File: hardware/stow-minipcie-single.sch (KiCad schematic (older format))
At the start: 2 parts

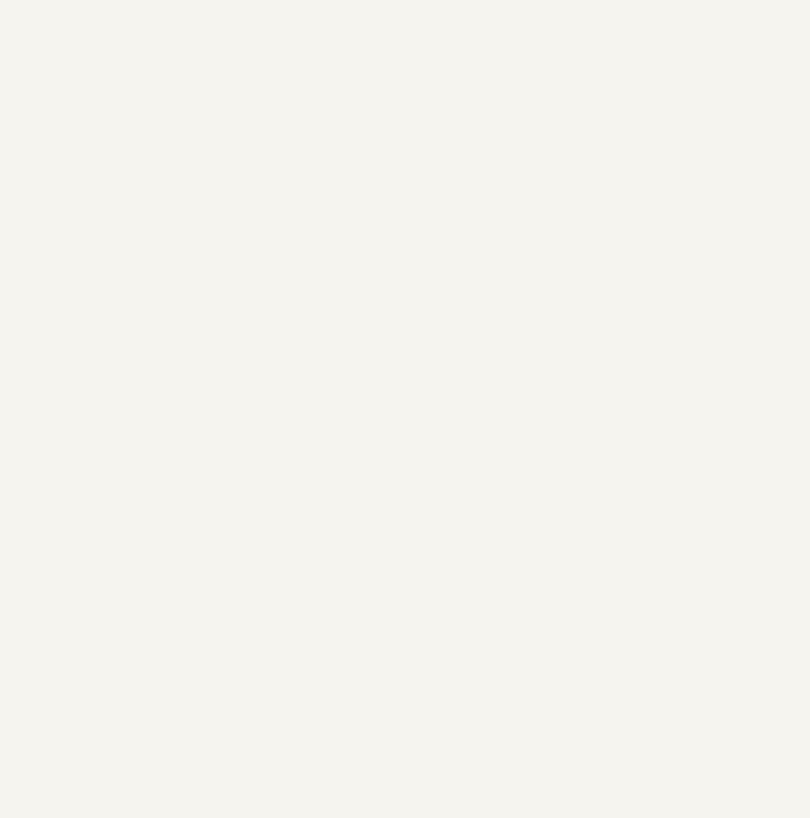
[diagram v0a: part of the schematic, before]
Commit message: Add FTDI chip to schematic.
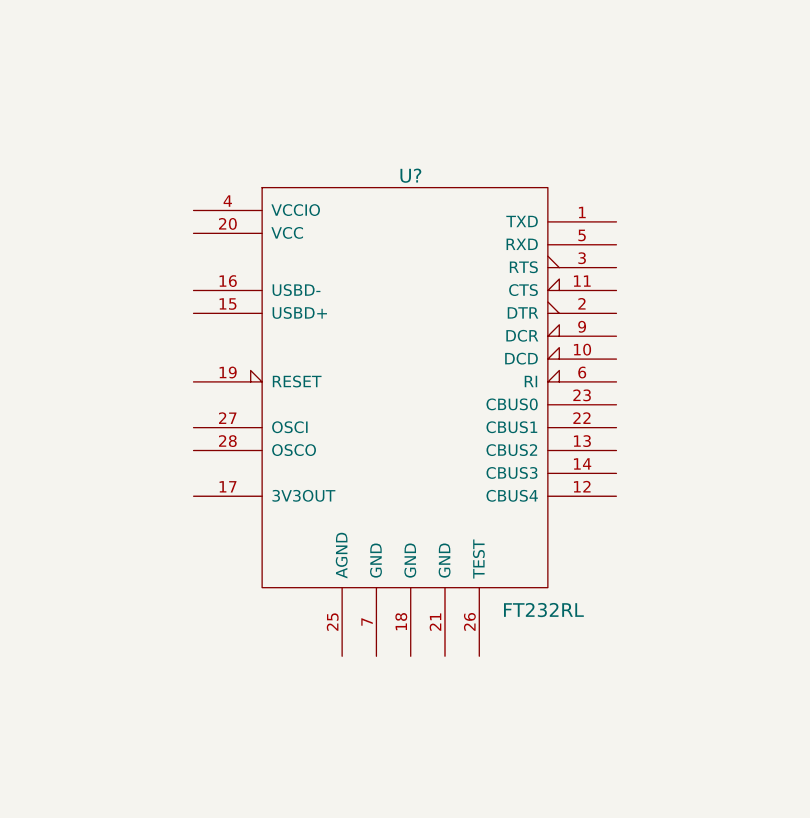
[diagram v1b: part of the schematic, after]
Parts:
- added U?: FT232RL, symbol FT232RL
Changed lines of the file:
@@
+	1    0    0    -1
+$EndComp
+$Comp
+L FT232RL U?
+U 1 1 55C1978C
+P 6150 3700
+F 0 "U?" H 6150 4600 60  0000 C CNN
+F 1 "FT232RL" H 6550 2700 60  0000 L CNN
+F 2 "" H 6150 3700 60  0000 C CNN
+F 3 "" H 6150 3700 60  0000 C CNN
+	1    6150 3700
 	1    0    0    -1
 $EndComp

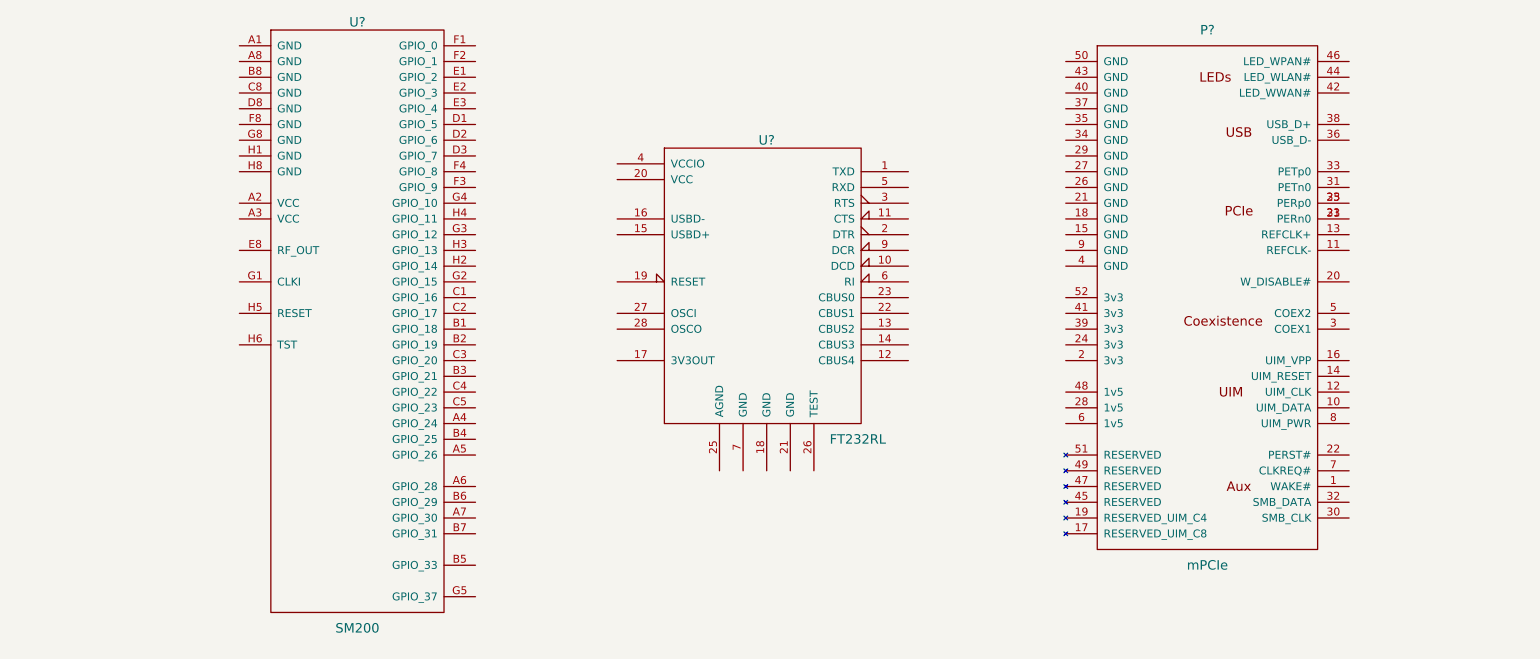
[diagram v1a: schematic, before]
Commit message: Add some schematic connections.
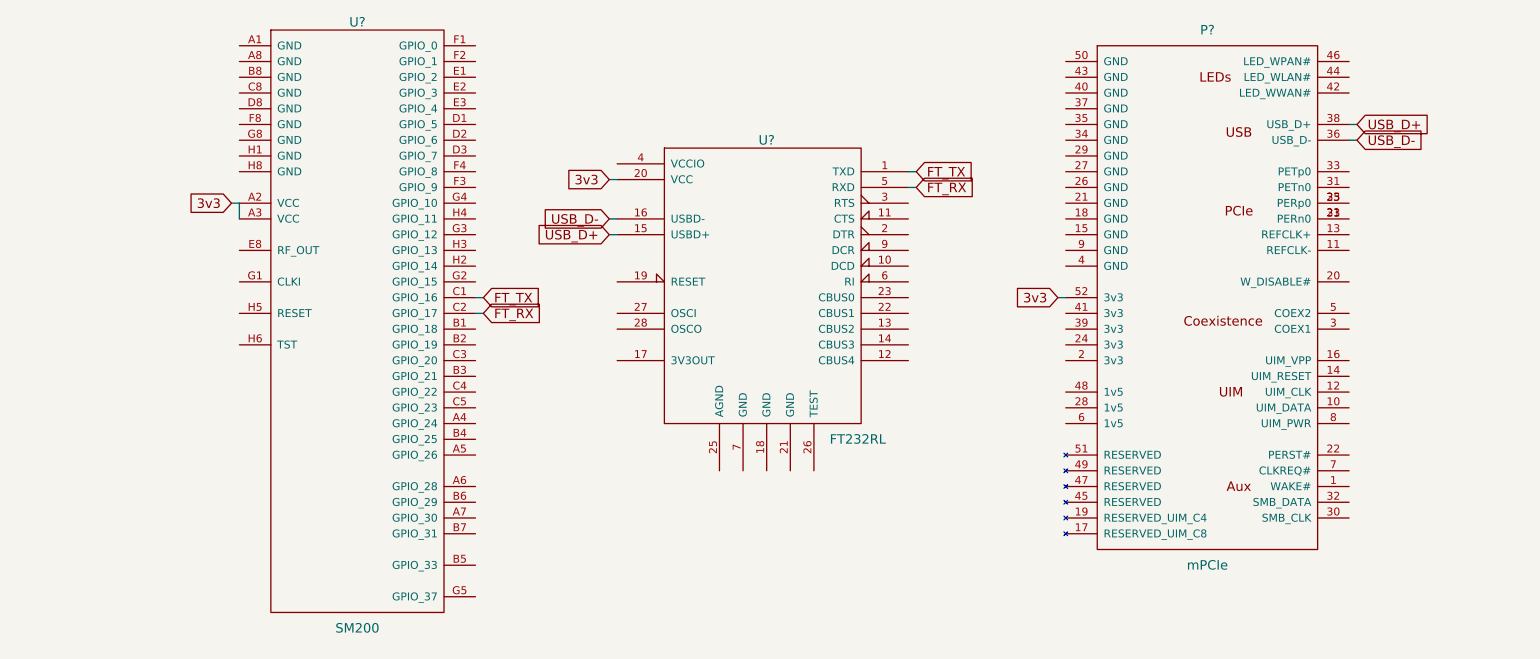
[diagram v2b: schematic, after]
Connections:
- net 3v3: now reaches U?.A2 (VCC)
- net 3v3: now also P?.52 (3v3), U?.20 (VCC), U?.A3 (VCC)
- net FT_TX: now reaches U?.C1 (GPIO_16)
- net FT_TX: now also U?.1 (TXD)
- net FT_RX: now reaches U?.C2 (GPIO_17)
- net FT_RX: now also U?.5 (RXD)
- net USB_D-: now reaches P?.36 (USB_D-)
- net USB_D-: now also U?.16 (USBD-)
- net USB_D+: now reaches P?.38 (USB_D+)
- net USB_D+: now also U?.15 (USBD+)
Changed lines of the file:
@@
 	1    0    0    -1
 $EndComp
+Text GLabel 9900 2700 2    60   Input ~ 0
+USB_D+
+Text GLabel 9900 2800 2    60   Input ~ 0
+USB_D-
+Text GLabel 5150 3400 0    60   Input ~ 0
+USB_D+
+Text GLabel 5150 3300 0    60   Input ~ 0
+USB_D-
+Text GLabel 5150 3050 0    60   Input ~ 0
+3v3
+Text GLabel 8000 3800 0    60   Input ~ 0
+3v3
+Text GLabel 2750 3200 0    60   Input ~ 0
+3v3
+Wire Wire Line
+	5150 3300 5200 3300
+Wire Wire Line
+	5150 3400 5200 3400
+Wire Wire Line
+	9850 2700 9900 2700
+Wire Wire Line
+	9850 2800 9900 2800
+Wire Wire Line
+	8000 3800 8050 3800
+Wire Wire Line
+	5150 3050 5200 3050
+Wire Wire Line
+	2750 3200 2800 3200
+Wire Wire Line
+	2800 3200 2800 3300
+Text GLabel 7100 3000 2    60   Input ~ 0
+FT_TX
+Text GLabel 7100 3100 2    60   Input ~ 0
+FT_RX
+Wire Wire Line
+	7050 3000 7100 3000
+Wire Wire Line
+	7100 3100 7050 3100
+Text GLabel 4350 3800 2    60   Input ~ 0
+FT_TX
+Text GLabel 4350 3900 2    60   Input ~ 0
+FT_RX
+Wire Wire Line
+	4300 3800 4350 3800
+Wire Wire Line
+	4300 3900 4350 3900
 $EndSCHEMATC

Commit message: Hooked up UART1 and RI.
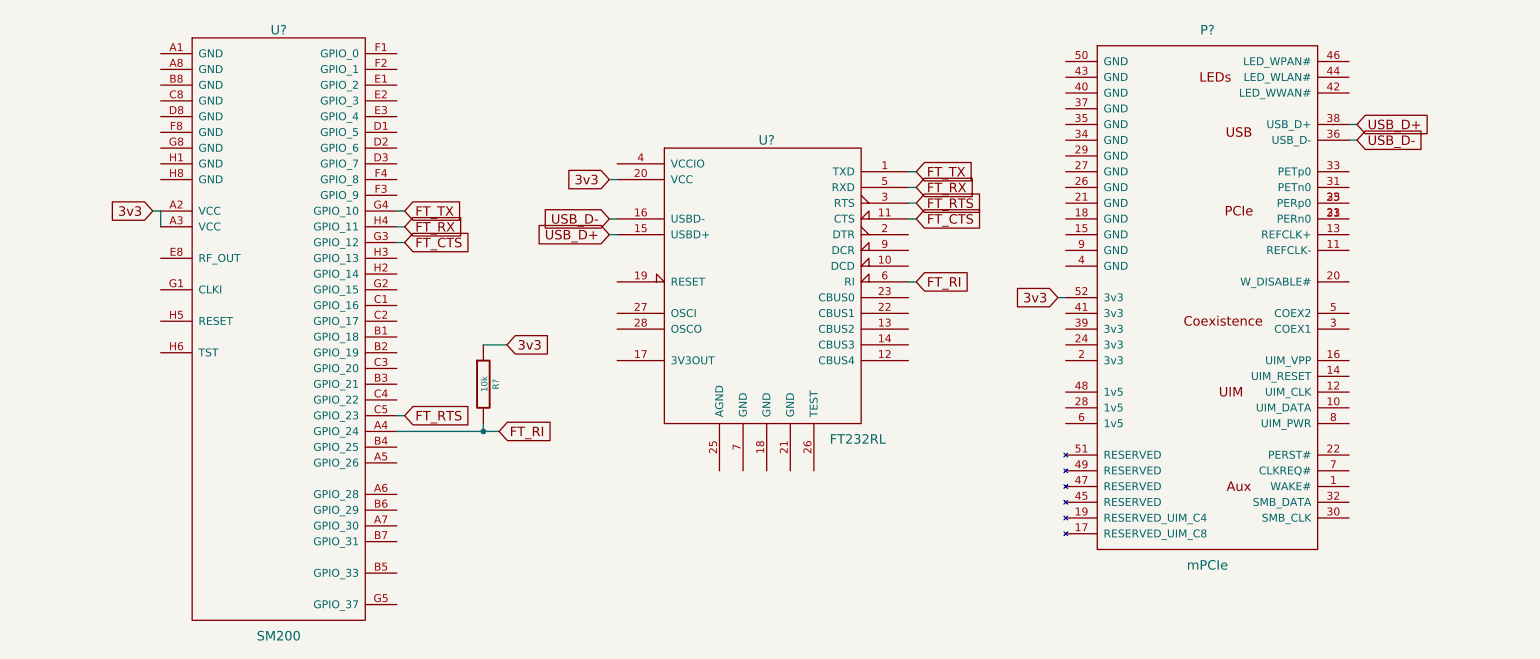
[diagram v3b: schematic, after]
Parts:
- added R?: 10k, symbol R
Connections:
- net 3v3: now also R?.1
- net FT_RX: now also U?.H4 (GPIO_11); no longer U?.C2 (GPIO_17)
- net FT_TX: now also U?.G4 (GPIO_10); no longer U?.C1 (GPIO_16)
- net FT_RI: now reaches U?.A4 (GPIO_24)
- net FT_RI: now also U?.6 (RI), R?.2
- net FT_RTS: now reaches U?.C5 (GPIO_23)
- net FT_RTS: now also U?.3 (RTS)
- net FT_CTS: now reaches U?.G3 (GPIO_12)
- net FT_CTS: now also U?.11 (CTS)
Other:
- moved on the sheet: U?
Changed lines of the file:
@@
 LIBS:valves
 LIBS:crumpschemes
+LIBS:stow-minipcie-single-cache
 EELAYER 25 0
 EELAYER END
@@
 L SM200 U?
 U 1 1 55C19545
-P 3550 3750
-F 0 "U?" H 3550 5450 60  0000 C CNN
-F 1 "SM200" H 3550 1600 60  0000 C CNN
-F 2 "" H 4250 5000 60  0000 C CNN
-F 3 "" H 4250 5000 60  0000 C CNN
-	1    3550 3750
+P 3050 3800
+F 0 "U?" H 3050 5500 60  0000 C CNN
+F 1 "SM200" H 3050 1650 60  0000 C CNN
+F 2 "" H 3750 5050 60  0000 C CNN
+F 3 "" H 3750 5050 60  0000 C CNN
+	1    3050 3800
 	1    0    0    -1
 $EndComp
@@
 Text GLabel 8000 3800 0    60   Input ~ 0
 3v3
-Text GLabel 2750 3200 0    60   Input ~ 0
+Text GLabel 2250 3250 0    60   Input ~ 0
 3v3
 Wire Wire Line
@@
 	5150 3050 5200 3050
 Wire Wire Line
-	2750 3200 2800 3200
+	2250 3250 2300 3250
 Wire Wire Line
-	2800 3200 2800 3300
+	2300 3250 2300 3350
 Text GLabel 7100 3000 2    60   Input ~ 0
 FT_TX
@@
 Wire Wire Line
 	7100 3100 7050 3100
-Text GLabel 4350 3800 2    60   Input ~ 0
+Text GLabel 3850 3250 2    60   Input ~ 0
 FT_TX
-Text GLabel 4350 3900 2    60   Input ~ 0
+Text GLabel 3850 3350 2    60   Input ~ 0
 FT_RX
+Text GLabel 7100 3300 2    60   Input ~ 0
+FT_CTS
+Text GLabel 7100 3200 2    60   Input ~ 0
+FT_RTS
 Wire Wire Line
-	4300 3800 4350 3800
+	7050 3200 7100 3200
 Wire Wire Line
-	4300 3900 4350 3900
+	7100 3300 7050 3300
+Text GLabel 3850 4550 2    60   Input ~ 0
+FT_RTS
+Text GLabel 3850 3450 2    60   Input ~ 0
+FT_CTS
+Wire Wire Line
+	3800 3250 3850 3250
+Wire Wire Line
+	3800 3350 3850 3350
+Wire Wire Line
+	3800 3450 3850 3450
+Wire Wire Line
+	3800 4550 3850 4550
+Text GLabel 7100 3700 2    60   Input ~ 0
+FT_RI
+Wire Wire Line
+	7050 3700 7100 3700
+Text GLabel 4450 4650 2    60   Input ~ 0
+FT_RI
+$Comp
+L R R?
+U 1 1 55FA5C22
+P 4350 4350
+F 0 "R?" V 4430 4350 40  0000 C CNN
+F 1 "10k" V 4357 4351 40  0000 C CNN
+F 2 "" V 4280 4350 30  0000 C CNN
+F 3 "" H 4350 4350 30  0000 C CNN
+	1    4350 4350
+	1    0    0    -1
+$EndComp
+Wire Wire Line
+	3800 4650 4450 4650
+Connection ~ 4350 4650
+Wire Wire Line
+	4350 4650 4350 4600
+Text GLabel 4500 4100 2    60   Input ~ 0
+3v3
+Wire Wire Line
+	4350 4100 4500 4100
 $EndSCHEMATC

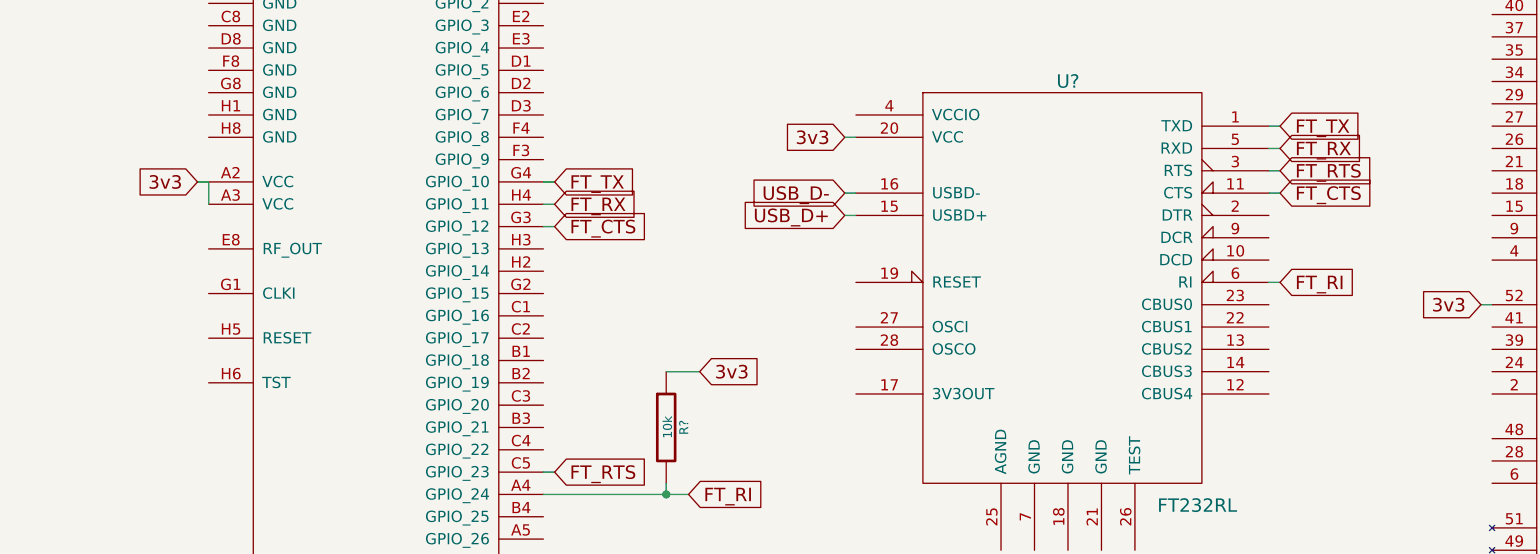
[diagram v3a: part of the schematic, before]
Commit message: Wired up RESET pin.
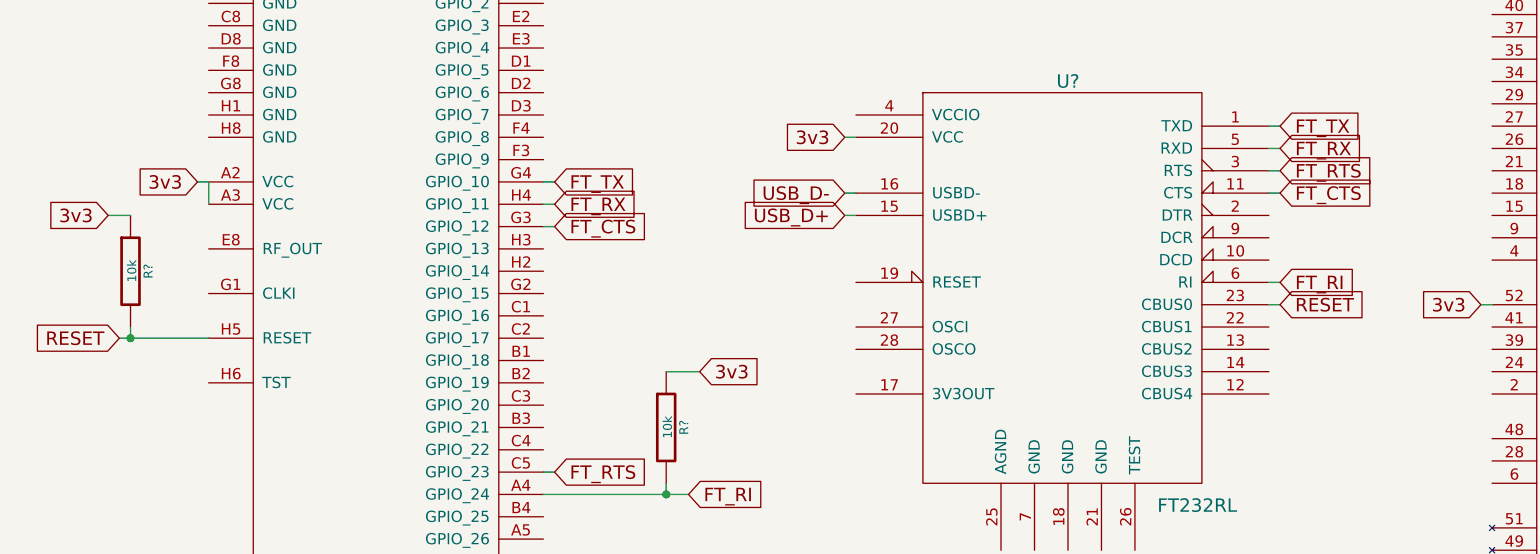
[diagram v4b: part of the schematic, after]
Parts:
- added R?: 10k, symbol R
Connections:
- net 3v3: now also R?.1
- net RESET: now reaches U?.H5 (RESET)
- net RESET: now also U?.23 (CBUS0), R?.2
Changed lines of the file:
@@
 Wire Wire Line
 	4350 4100 4500 4100
+Text GLabel 7100 3800 2    60   Input ~ 0
+RESET
+Wire Wire Line
+	7050 3800 7100 3800
+Text GLabel 1900 3950 0    60   Input ~ 0
+RESET
+$Comp
+L R R?
+U 1 1 55FA6083
+P 1950 3650
+F 0 "R?" V 2030 3650 40  0000 C CNN
+F 1 "10k" V 1957 3651 40  0000 C CNN
+F 2 "" V 1880 3650 30  0000 C CNN
+F 3 "" H 1950 3650 30  0000 C CNN
+	1    1950 3650
+	1    0    0    -1
+$EndComp
+Text GLabel 1850 3400 0    60   Input ~ 0
+3v3
+Wire Wire Line
+	1900 3950 2300 3950
+Wire Wire Line
+	1950 3950 1950 3900
+Connection ~ 1950 3950
+Wire Wire Line
+	1850 3400 1950 3400
 $EndSCHEMATC

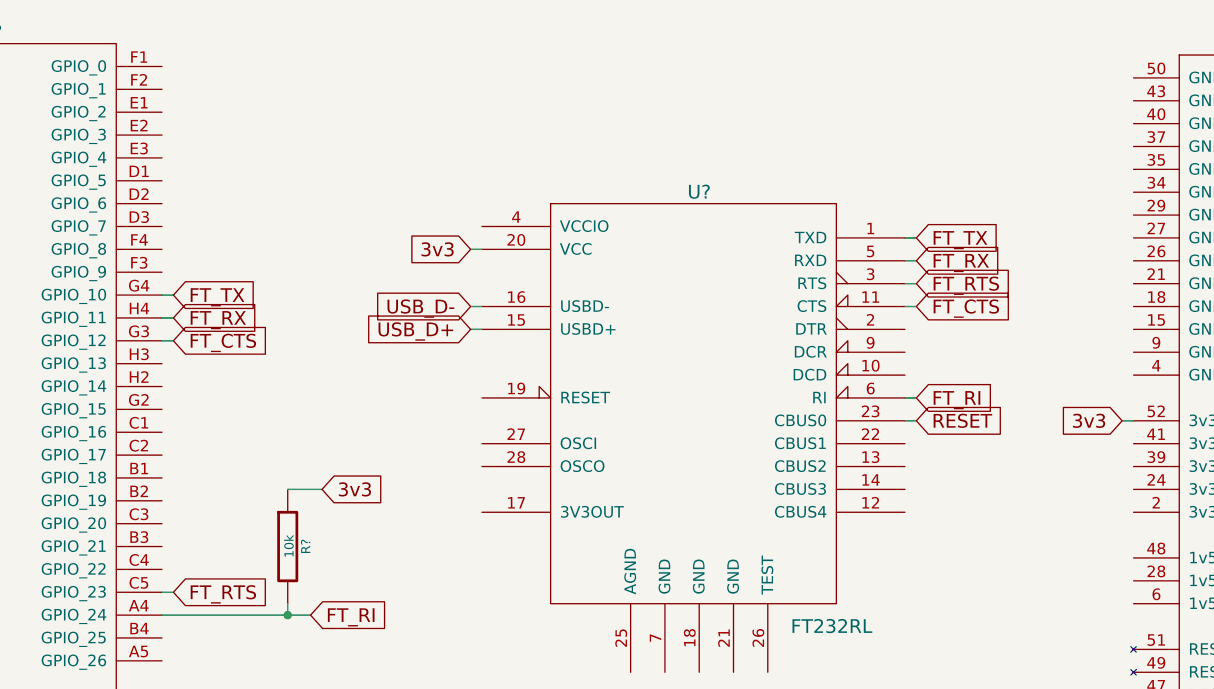
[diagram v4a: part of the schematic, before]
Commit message: Wire up PWREN and SLEEP pin.
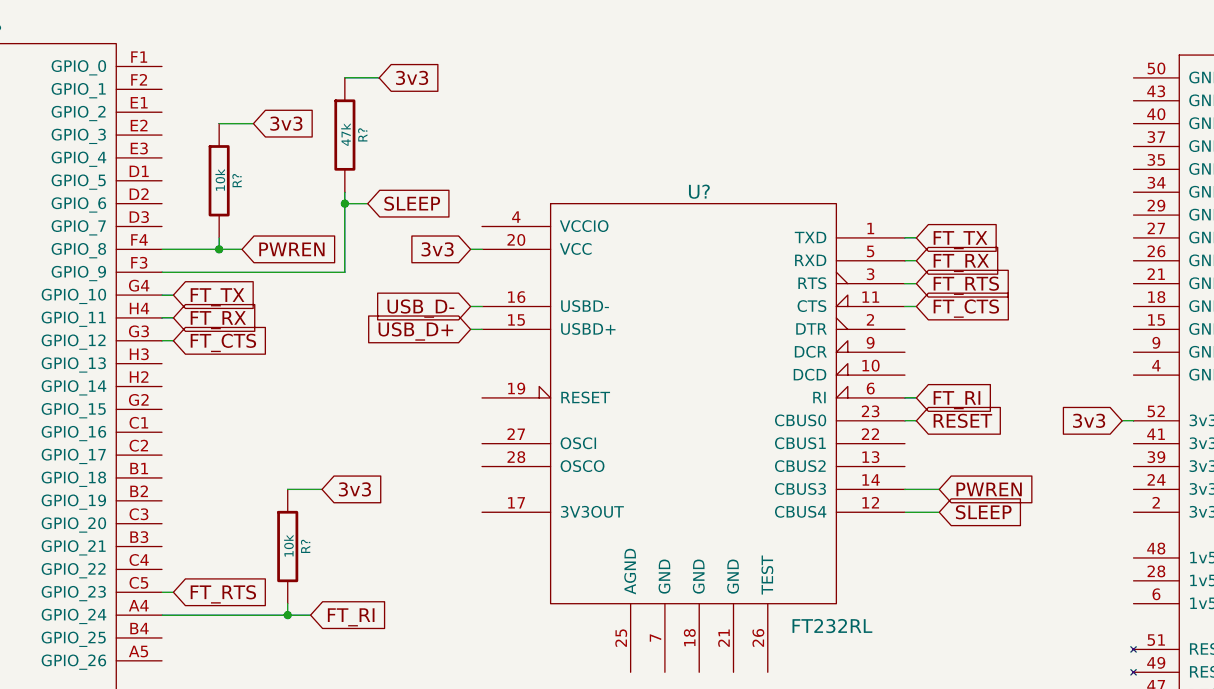
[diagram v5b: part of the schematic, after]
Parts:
- added R?: 10k, symbol R
- added R?: 47k, symbol R
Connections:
- net 3v3: now also R?.1, R?.1
- net SLEEP: now reaches U?.F3 (GPIO_9)
- net SLEEP: now also U?.12 (CBUS4), R?.2
- net PWREN: now reaches U?.F4 (GPIO_8)
- net PWREN: now also U?.14 (CBUS3), R?.2
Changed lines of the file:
@@
 Wire Wire Line
 	1850 3400 1950 3400
+Text GLabel 7200 4100 2    60   Input ~ 0
+PWREN
+Text GLabel 7200 4200 2    60   Input ~ 0
+SLEEP
+Text GLabel 4150 3050 2    60   Input ~ 0
+PWREN
+$Comp
+L R R?
+U 1 1 55FA6345
+P 4050 2750
+F 0 "R?" V 4130 2750 40  0000 C CNN
+F 1 "10k" V 4057 2751 40  0000 C CNN
+F 2 "" V 3980 2750 30  0000 C CNN
+F 3 "" H 4050 2750 30  0000 C CNN
+	1    4050 2750
+	1    0    0    -1
+$EndComp
+Connection ~ 4050 3050
+Wire Wire Line
+	4050 3050 4050 3000
+Text GLabel 4200 2500 2    60   Input ~ 0
+3v3
+Wire Wire Line
+	4050 2500 4200 2500
+Wire Wire Line
+	3800 3050 4150 3050
+Wire Wire Line
+	7050 4100 7200 4100
+Wire Wire Line
+	7050 4200 7200 4200
+Text GLabel 4700 2850 2    60   Input ~ 0
+SLEEP
+$Comp
+L R R?
+U 1 1 55FA6654
+P 4600 2550
+F 0 "R?" V 4680 2550 40  0000 C CNN
+F 1 "47k" V 4607 2551 40  0000 C CNN
+F 2 "" V 4530 2550 30  0000 C CNN
+F 3 "" H 4600 2550 30  0000 C CNN
+	1    4600 2550
+	1    0    0    -1
+$EndComp
+Connection ~ 4600 2850
+Wire Wire Line
+	4600 2800 4600 3150
+Text GLabel 4750 2300 2    60   Input ~ 0
+3v3
+Wire Wire Line
+	4600 2300 4750 2300
+Wire Wire Line
+	4700 2850 4600 2850
+Wire Wire Line
+	4600 3150 3800 3150
 $EndSCHEMATC
